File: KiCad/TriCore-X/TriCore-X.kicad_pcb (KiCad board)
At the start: 6 copper layers, 100 x 100 mm, 119 parts, among them J1 PJ-035DH, J2 877159106, J3 HDMI_A, Q1 AOD407, U1 RK3568B2, U10 USB3300-EZK-TR, U2 XC7A100T-FGG484, U3 TPS56637RPAR, U4 TPS56637RPAR, U5 RK809-5, U6 JFM38U1B-B313-4F, U7 STM32H723VGHx, U8 IS43LQ32256AL-062BLI, U9 TPD12S016RKTR, Y1 32.768KHZ, Y2 Crystal_GND24

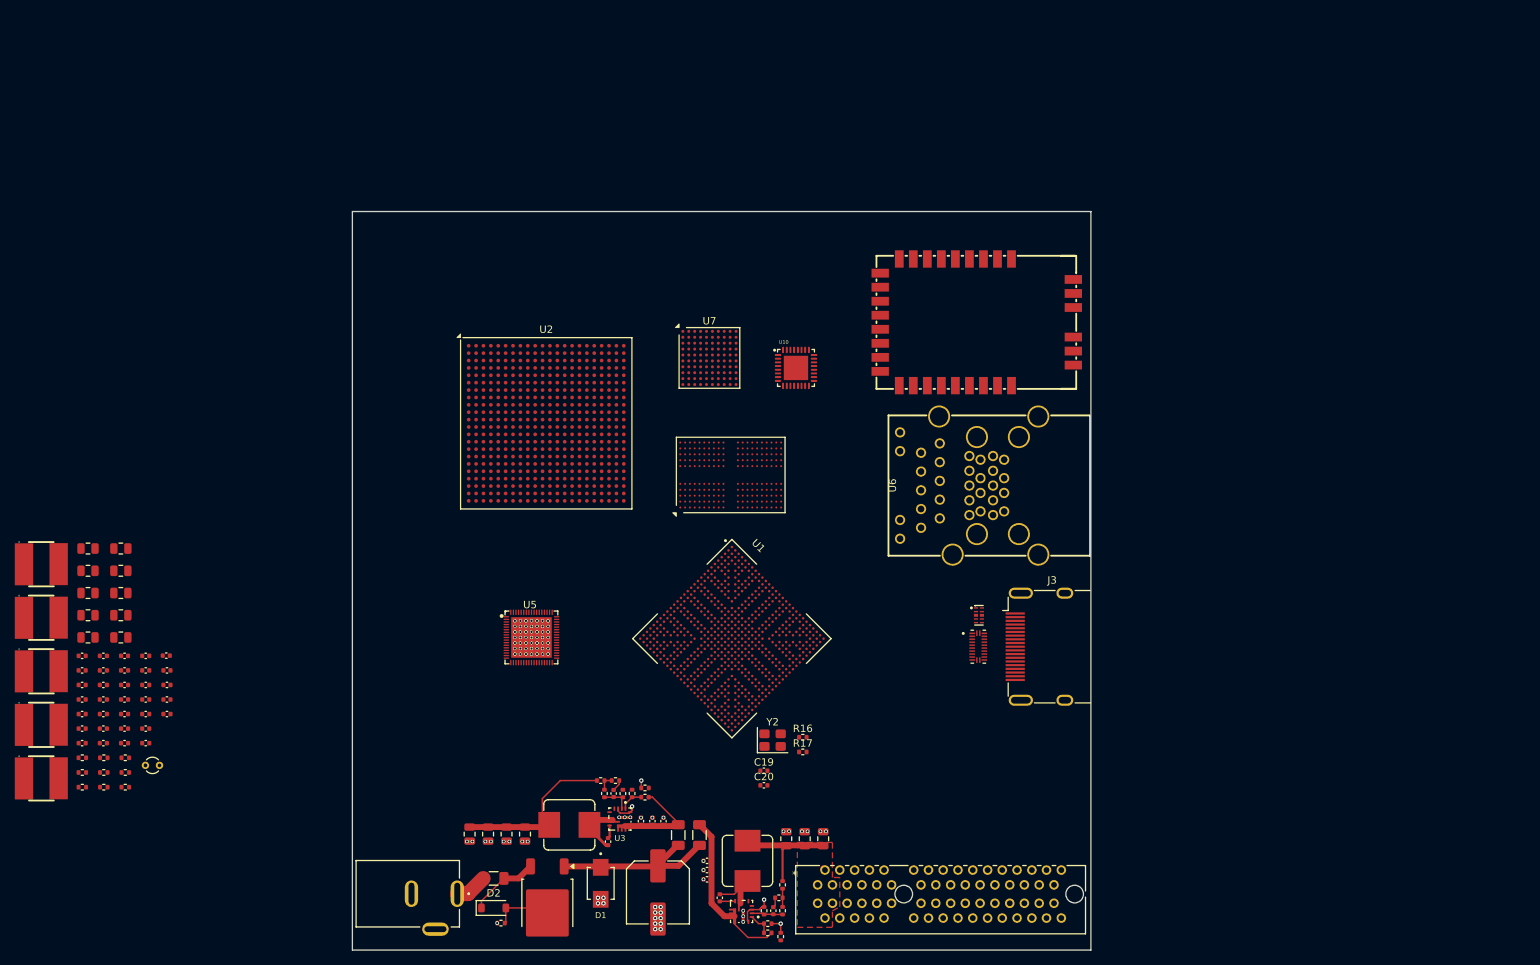
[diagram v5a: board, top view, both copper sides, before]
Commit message: refactor: update schematic components and library references, including STM32H743 and new power symbols
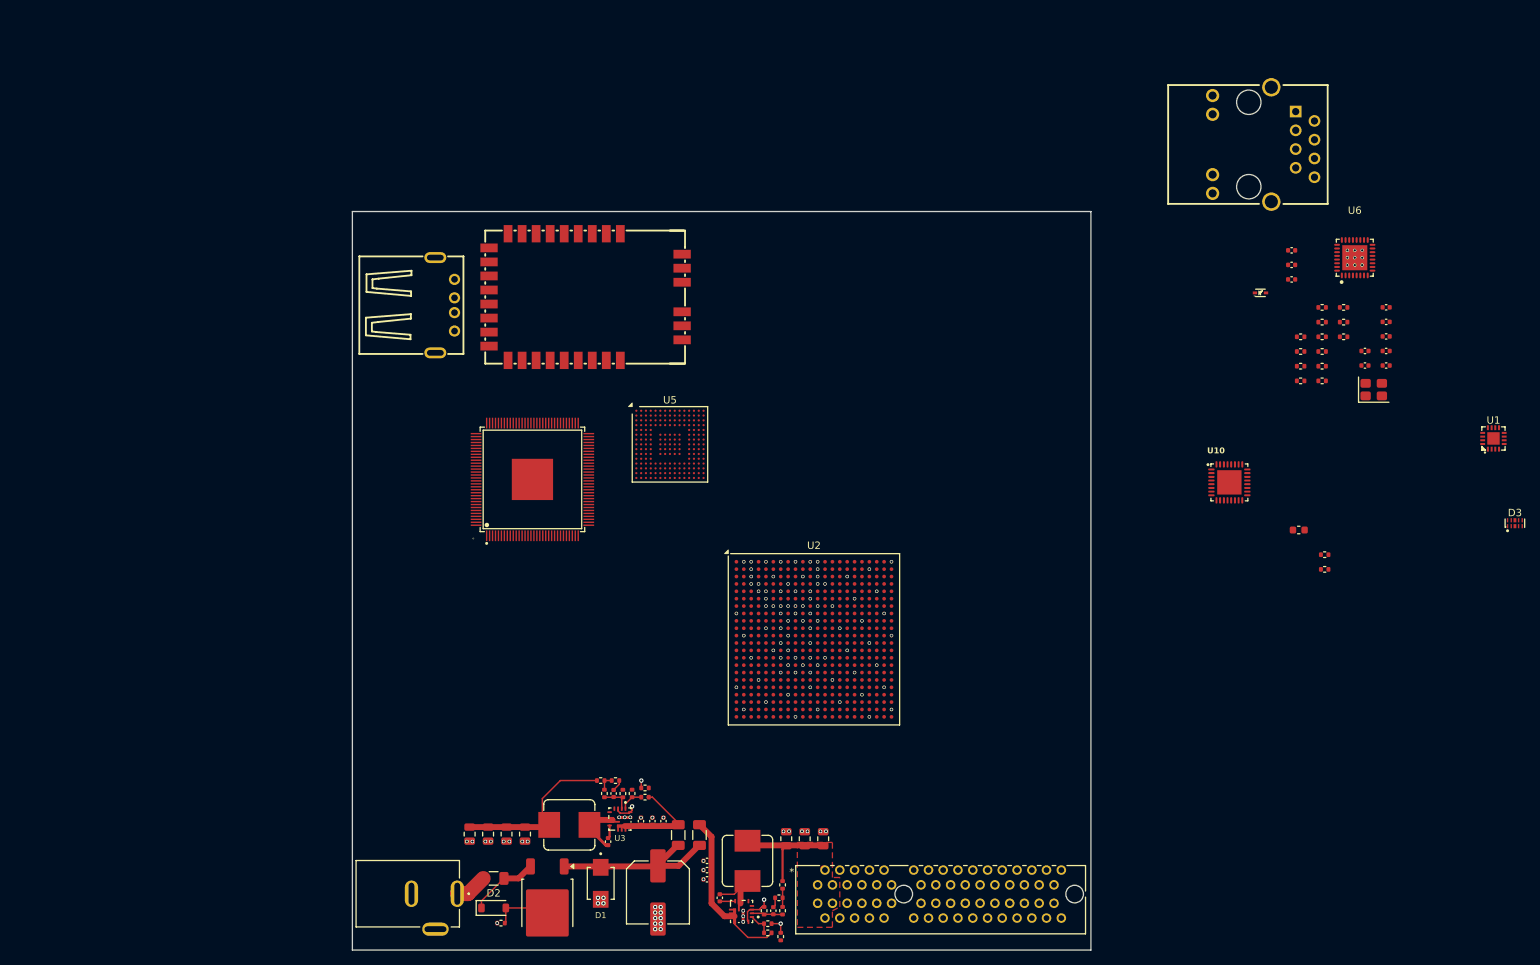
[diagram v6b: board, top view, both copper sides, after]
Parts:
- removed C29, C30, C31, C32, C33, C34, C35, C36, C37, C40, C41, C42, C43, C45: 1uF, Capacitor_SMD:C_0402_1005Metric
- removed C38, C39: 2.2uF, Capacitor_SMD:C_0402_1005Metric
- removed C44, C46, C47, C48, C49, C50: 10uF, Capacitor_SMD:C_0402_1005Metric
- removed C51, C52, C53, C54, C55, C56, C57, C58, C59, C60: 22uF, Capacitor_SMD:C_0805_2012Metric
- removed C61, C62, C63: 100nF, Capacitor_SMD:C_0402_1005Metric
- removed L3, L4, L5, L6, L7: FNR6045SR47NT, L_6045:IND-SMD_L6.0-W6.0_FNR60XXS
- removed U8: IS43LQ32256AL-062BLI, Package_BGA:BGA-200_10x14.5mm_Layout12x22_P0.8x0.65mm
- removed U9: TPD12S016RKTR, TPD12S016RKTR:IC_TPD12S016RKTR
- removed Y2: Crystal_GND24, Crystal:Crystal_SMD_3225-4Pin_3.2x2.5mm
- added D5: LESD5D5.0CT1G, LESD5D5.0CT1G:SOD-523_L1.2-W0.8-LS1.6-BI, F.Cu at (216.7, 56.8)
- added FB1: 220R@100M, Inductor_SMD:L_0603_1608Metric, F.Cu at (221.9, 89.0)
- added R27: 22R, Resistor_SMD:R_0402_1005Metric, F.Cu at (225.1, 68.8)
- added R28: 22R, Resistor_SMD:R_0402_1005Metric, F.Cu at (228.0, 58.8)
- added R29: 4.7k, Resistor_SMD:R_0402_1005Metric, F.Cu at (228.0, 60.8)
- added R30: 4.7k, Resistor_SMD:R_0402_1005Metric, F.Cu at (228.0, 62.8)
- added USB1: AF 90° ZJDG ZB, USB-A:USB-A-TH_AF-90-ZJDG-ZB, F.Cu at (101.8, 58.5)
- C14, C4: value 0.1uF -> 100nF
- C19: value 18pF -> 1nF/50V
- C20: value 18pF -> 10nF
- C21: value 1uF -> 10nF
- C22, C25, C27: value 1uF -> 100nF
- C23, C24: value 1uF -> 15pF
- C26, C28: value 1uF -> 10uF
- J3: value HDMI_A -> HR911105A_C12074; footprint Connector_Video:HDMI_A_Molex_208658-1001_Horizontal -> RJ45:RJ45-TH_HR911105A
- R16: value 1M -> 510R
- R17: value 22R -> 510R
- R18: value 82K -> 4.7k
- R19: value 120K -> 1.5k
- R20: value 4.7K -> 1.5k
- R21: value 4.7K -> 4.7k
- R22: value 100K -> 4.7k
- R23: value 22K -> 4.7k
- R24: value 10K -> 2.49k
- R25, R26: value 10K -> 22R
- U1: value RK3568B2 -> CH334P; footprint RK3568B2:BGA636C65P28X28_1900X1900X111 -> CH334P:QFN-16_L3.0-W3.0-P0.50-BL-EP1.7
- U5: value RK809-5 -> STM32H743IIKx; footprint RK809-5:QFN-68_L7.0-W7.0-P0.35-BL-EP5.5 -> Package_BGA:UFBGA-201_10x10mm_Layout15x15_P0.65mm
- U6: value JFM38U1B-B313-4F -> RTL8201F-VB-CG; footprint JFM38U1B-B313-4F:RJ45-TH_JFM38U11-B31X-4F -> RTL8201F-VB-CG:QFN-32_L5.0-W5.0-P0.50-BL-EP3.4
- U7: value STM32H723VGHx -> T113-S3_C5197687; footprint Package_BGA:TFBGA-100_8x8mm_Layout10x10_P0.8mm -> T113-S3:LQFP-128_L14.0-W14.0-P0.40-LS16.0-BL-EP5.6
- Y1: value 32.768KHZ -> 25Mhz; footprint Crystal:Crystal_DS26_D2.0mm_L6.0mm_Vertical -> Crystal:Crystal_SMD_3225-4Pin_3.2x2.5mm
- moved C24 184.4 mm to (233.7, 58.8)
- moved C25 184.4 mm to (233.7, 60.8)
- moved C26 184.4 mm to (233.7, 62.7)
- moved C27 184.4 mm to (233.7, 64.7)
- moved C22 179.0 mm to (230.9, 64.7)
- moved C23 179.0 mm to (230.9, 66.7)
- moved C28 178.1 mm to (233.7, 66.7)
- moved R22 176.6 mm to (225.1, 58.8)
- moved R23 176.6 mm to (225.1, 60.8)
- moved R18 174.5 mm to (222.2, 62.8)
- moved R19 174.5 mm to (222.2, 64.8)
- moved R20 174.5 mm to (222.2, 66.8)
- moved Y1 173.9 mm to (232.1, 69.9)
- moved R24 171.8 mm to (225.1, 62.8)
- moved R25 171.8 mm to (225.1, 64.8)
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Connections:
- C19 pad 1: Net-(C19-Pad1) -> GND
- C19 pad 2: GND -> Net-(J3-CHSGND)
- C20 pad 2: Net-(U1F-XIN24M) -> Net-(C20-Pad2)
- C21 pad 1: /power/VSWOUT2 -> GND
- C21 pad 2: GND -> Net-(C21-Pad2)
- C22 pad 1: /power/BUCK5 -> Net-(U6-DVDD10OUT)
- C23 pad 1: /power/VCC SYS -> GND
- C23 pad 2: GND -> Net-(U6-CKXTAL2)
- C24 pad 1: /power/VLDOI -> GND
- C24 pad 2: GND -> Net-(U6-CKXTAL1)
- C25 pad 1: /power/VLDO2 -> GND
- C25 pad 2: GND -> Net-(U6-AVDD10OUT)
- C26 pad 1: /power/VLDO3 -> Ethernet_3V3
- C27 pad 1: /power/BUCK 5 -> Ethernet_3V3
- C28 pad 1: /power/VLDO4 -> Ethernet_3V3
- J3 pad 1: unconnected-(J3-D2+-Pad1) -> /Expansion_Port/ETH_TX_P
- J3 pad 10: unconnected-(J3-CK+-Pad10) -> Net-(J3-Pad10)
- J3 pad 11: unconnected-(J3-CKS-Pad11) -> GND
- J3 pad 12: unconnected-(J3-CK--Pad12) -> Net-(J3-Pad12)
- J3 pad 2: unconnected-(J3-D2S-Pad2) -> /Expansion_Port/ETH_TX_N
- J3 pad 3: unconnected-(J3-D2--Pad3) -> /Expansion_Port/ETH_RX_P
- J3 pad 4: unconnected-(J3-D1+-Pad4) -> Net-(C20-Pad2)
- J3 pad 5: unconnected-(J3-D1S-Pad5) -> Net-(C21-Pad2)
- J3 pad 6: unconnected-(J3-D1--Pad6) -> /Expansion_Port/ETH_RX_N
- J3 pad 8: unconnected-(J3-D0S-Pad8) -> Net-(J3-CHSGND)
- J3 pad 9: unconnected-(J3-D0--Pad9) -> Ethernet_3V3
- R16 pad 1: Net-(U1F-XIN24M) -> /Expansion_Port/LED_ACT
- R16 pad 2: Net-(U1F-XOUT24M) -> Net-(J3-Pad10)
- R17 pad 1: Net-(U1F-XOUT24M) -> /Expansion_Port/LED_LINK
- R17 pad 2: Net-(C19-Pad1) -> Net-(J3-Pad12)
- R18 pad 1: Net-(U5-FB3) -> /Expansion_Port/LED_ACT
- R18 pad 2: /power/BUCK3 -> Ethernet_3V3
- R19 pad 1: GND -> PHY_MDIO
- R19 pad 2: Net-(U5-FB3) -> Ethernet_3V3
- R20 pad 1: /power/BUCK4 -> PHY_MDC
- R20 pad 2: /power/RK809-5_SCL -> Ethernet_3V3
- R21 pad 1: /power/BUCK4 -> PHY_RSTN
- R21 pad 2: /power/RK809-5_SDA -> Ethernet_3V3
- R22 pad 1: +5V -> PHY_RXER
- R22 pad 2: Net-(U5-VDC) -> GND
- R23 pad 1: Net-(U5-VDC) -> /Expansion_Port/LED_LINK
- R24 pad 1: /power/BUCK4 -> GND
- R24 pad 2: Net-(U5-INT) -> Net-(U6-RSET)
- R25 pad 1: Net-(U5-CLK32K) -> /Expansion_Port/ETH_TX_P
- R25 pad 2: /power/BUCK4 -> Net-(U6-MDI+[0])
- R26 pad 1: Net-(U5-RESETB) -> /Expansion_Port/ETH_TX_N
- R26 pad 2: /power/BUCK4 -> Net-(U6-MDI-[0])
- U6 pad 1: unconnected-(U6-VBUS-Pad1) -> Net-(U6-RSET)
- U6 pad 10: unconnected-(U6-VBUS-Pad10) -> PHY_RXD1
- U6 pad 13: GND -> unconnected-(U6-RXC-Pad13)
- U6 pad 14: unconnected-(U6-STDA_SSRX--Pad14) -> Ethernet_3V3
- U6 pad 15: unconnected-(U6-STDA_SSRX+-Pad15) -> PHY_TXCLK
- U6 pad 16: GND -> PHY_TXD0
- U6 pad 17: unconnected-(U6-SRDA_SSTX--Pad17) -> PHY_TXD1
- U6 pad 2: unconnected-(U6-D--Pad2) -> Net-(U6-AVDD10OUT)
- U6 pad 20: unconnected-(U6-D1+-Pad20) -> PHY_TXEN
- U6 pad 21: unconnected-(U6-D1--Pad21) -> PHY_RSTN
- U6 pad 22: unconnected-(U6-D2+-Pad22) -> PHY_MDC
- U6 pad 23: unconnected-(U6-D2--Pad23) -> PHY_MDIO
- U6 pad 24: unconnected-(U6-D3+-Pad24) -> /Expansion_Port/LED_ACT
- U6 pad 25: unconnected-(U6-D3--Pad25) -> /Expansion_Port/LED_LINK
- U6 pad 26: unconnected-(U6-D4+-Pad26) -> PHY_CRS_DV
- U6 pad 28: GND -> PHY_RXER
- U6 pad 29: unconnected-(U6-LED-G+-Pad29) -> Net-(U6-DVDD10OUT)
- U6 pad 3: unconnected-(U6-D+-Pad3) -> Net-(U6-MDI+[0])
- U6 pad 30: unconnected-(U6-LED-D--Pad30) -> Ethernet_3V3
- U6 pad 31: unconnected-(U6-LED-Y+-Pad31) -> Net-(U6-CKXTAL1)
- U6 pad 32: unconnected-(U6-LED-Y--Pad32) -> Net-(U6-CKXTAL2)
- U6 pad 33: unconnected-(U6-SHELL-Pad33) -> GND
- U6 pad 4: GND -> Net-(U6-MDI-[0])
- U6 pad 5: unconnected-(U6-STDA_SSRX--Pad5) -> Net-(U6-MDI+[1])
- U6 pad 6: unconnected-(U6-STDA_SSRX+-Pad6) -> Net-(U6-MDI-[1])
- U6 pad 7: GND -> Ethernet_3V3
- U6 pad 8: unconnected-(U6-SRDA_SSTX--Pad8) -> Net-(U6-RXDV)
- U6 pad 9: unconnected-(U6-STDA_SSTX+-Pad9) -> PHY_RXD0
- Y1 pad 1: Net-(U5-XOUT) -> Net-(U6-CKXTAL1)
- Y1 pad 2: Net-(U5-XIN) -> GND
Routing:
- net GND: vias 90 -> 137

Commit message: refactor: update schematic components, remove unused files, and add new LED and CH334P symbols
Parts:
- removed WIFI1: BL-M8822CU3-A, BL-M8822CU3-A:WIRELM-SMD_BL-M8822CU3-A
- added B1: CR2032-BS-2-1, Battery Holder BS-2-1:BAT-TH_BS-2-1, F.Cu at (121.8, 30.0)
- added C29: 22uF, Capacitor_SMD:C_0805_2012Metric, F.Cu at (124.8, 108.7)
- added C30: 100nF, Capacitor_SMD:C_0402_1005Metric, F.Cu at (121.5, 112.2)
- added C31: 22uF, Capacitor_SMD:C_0805_2012Metric, F.Cu at (119.8, 112.2)
- added C32: 22uF, Capacitor_SMD:C_0805_2012Metric, F.Cu at (119.5, 103.9)
- added C33: 100nF, Capacitor_SMD:C_0402_1005Metric, F.Cu at (121.3, 104.2)
- added C34: 22uF, Capacitor_SMD:C_0805_2012Metric, F.Cu at (124.8, 100.4)
- added C35: 22uF, Capacitor_SMD:C_0805_2012Metric, F.Cu at (119.5, 94.9)
- added C36: 100nF, Capacitor_SMD:C_0402_1005Metric, F.Cu at (121.2, 95.0)
- added C37: 22uF, Capacitor_SMD:C_0805_2012Metric, F.Cu at (124.7, 91.5)
- added C38: 22uF, Capacitor_SMD:C_0805_2012Metric, F.Cu at (119.7, 86.9)
- added C39: 100nF, Capacitor_SMD:C_0402_1005Metric, F.Cu at (121.5, 87.1)
- added C40: 22uF, Capacitor_SMD:C_0805_2012Metric, F.Cu at (125.0, 83.5)
- added C41: 1uF, Capacitor_SMD:C_0402_1005Metric, F.Cu at (104.2, 91.8)
- added C42: 1uF, Capacitor_SMD:C_0402_1005Metric, F.Cu at (100.5, 91.9)
- added C43: 1uF, Capacitor_SMD:C_0402_1005Metric, F.Cu at (104.2, 86.2)
- added C44: 1uF, Capacitor_SMD:C_0402_1005Metric, F.Cu at (100.5, 86.2)
- added C45: 22uF, Capacitor_SMD:C_0805_2012Metric, F.Cu at (122.0, 108.0)
- added C46: 22uF, Capacitor_SMD:C_0805_2012Metric, F.Cu at (122.0, 99.7)
- added C47: 22uF, Capacitor_SMD:C_0805_2012Metric, F.Cu at (122.0, 90.8)
- added C48: 22uF, Capacitor_SMD:C_0805_2012Metric, F.Cu at (122.2, 82.8)
- added C49: 100nF, Capacitor_SMD:C_0402_1005Metric, F.Cu at (146.0, 27.6)
- added C50: 2.2uF, Capacitor_SMD:C_0402_1005Metric, F.Cu at (146.0, 29.5)
- added C51: 2.2uF, Capacitor_SMD:C_0402_1005Metric, F.Cu at (146.0, 31.5)
- added C52: 100nF, Capacitor_SMD:C_0402_1005Metric, B.Cu at (150.8, 53.3)
- added C53: 100nF, Capacitor_SMD:C_0402_1005Metric, F.Cu at (146.0, 33.5)
- added C54: 1uF, Capacitor_SMD:C_0402_1005Metric, F.Cu at (146.0, 35.4)
- added C55: 100nF, Capacitor_SMD:C_0402_1005Metric, B.Cu at (150.8, 55.2)
- added C56: 100nF, Capacitor_SMD:C_0402_1005Metric, B.Cu at (150.8, 57.2)
- added C57: 100nF, Capacitor_SMD:C_0402_1005Metric, B.Cu at (150.8, 59.2)
- added C58: 100nF, Capacitor_SMD:C_0402_1005Metric, B.Cu at (150.8, 61.2)
- added C59: 100nF, Capacitor_SMD:C_0402_1005Metric, B.Cu at (147.9, 53.3)
- added C60: 100nF, Capacitor_SMD:C_0402_1005Metric, B.Cu at (147.9, 55.2)
- added C61: 100nF, Capacitor_SMD:C_0402_1005Metric, B.Cu at (147.9, 57.2)
- added C62: 100nF, Capacitor_SMD:C_0402_1005Metric, B.Cu at (147.9, 59.2)
- added C63: 100nF, Capacitor_SMD:C_0402_1005Metric, B.Cu at (147.9, 61.2)
- added C64: 100nF, Capacitor_SMD:C_0402_1005Metric, B.Cu at (145.0, 53.3)
- added C65: 100nF, Capacitor_SMD:C_0402_1005Metric, B.Cu at (145.0, 55.2)
- added C66: 100nF, Capacitor_SMD:C_0402_1005Metric, B.Cu at (145.0, 57.2)
- added C67: 100nF, Capacitor_SMD:C_0402_1005Metric, B.Cu at (145.0, 59.2)
- added C68: 100nF, Capacitor_SMD:C_0402_1005Metric, B.Cu at (145.0, 61.2)
- added C69: 100nF, Capacitor_SMD:C_0402_1005Metric, B.Cu at (142.2, 53.3)
- added C70: 100nF, Capacitor_SMD:C_0402_1005Metric, B.Cu at (142.2, 55.2)
- added C71: 100nF, Capacitor_SMD:C_0402_1005Metric, B.Cu at (142.2, 57.2)
- added C72: 100nF, Capacitor_SMD:C_0402_1005Metric, B.Cu at (141.8, 59.8)
- added C73: 100nF, Capacitor_SMD:C_0402_1005Metric, B.Cu at (141.0, 61.2)
- added C74: 100nF, Capacitor_SMD:C_0402_1005Metric, B.Cu at (138.0, 61.5)
- added D10: LED, LED_SMD:LED_0603_1608Metric, F.Cu at (68.5, 85.2)
- added D11: SS14, Diode_SMD:D_SMA, F.Cu at (106.2, 38.0)
- added D4: ESD224DQAR, ESD224DQAR:USON-10_L2.5-W1.0-P0.50-BL, F.Cu at (104.8, 75.8)
- added D6: LED, LED_SMD:LED_0603_1608Metric, F.Cu at (68.5, 74.8)
- added D7: LED, LED_SMD:LED_0603_1608Metric, F.Cu at (68.5, 77.4)
- added D8: LED, LED_SMD:LED_0603_1608Metric, F.Cu at (68.5, 80.0)
- added D9: LED, LED_SMD:LED_0603_1608Metric, F.Cu at (68.5, 82.6)
- added L3: FWP252012P-1R0ML, FWP252012P-1R0ML:IND-SMD_L2.5-W2.0_YXMBL252010P, F.Cu at (124.0, 113.0)
- added L4: FWP252012P-1R0ML, FWP252012P-1R0ML:IND-SMD_L2.5-W2.0_YXMBL252010P, F.Cu at (124.0, 104.7)
- added L5: FWP252012P-1R0ML, FWP252012P-1R0ML:IND-SMD_L2.5-W2.0_YXMBL252010P, F.Cu at (124.0, 95.8)
- added L6: FWP252012P-1R0ML, FWP252012P-1R0ML:IND-SMD_L2.5-W2.0_YXMBL252010P, F.Cu at (124.2, 87.6)
- added R31: 68K, Resistor_SMD:R_0402_1005Metric, F.Cu at (126.5, 110.3)
- added R32: 20K, Resistor_SMD:R_0402_1005Metric, F.Cu at (126.5, 102.0)
- added R33: 15K, Resistor_SMD:R_0402_1005Metric, F.Cu at (126.5, 108.3)
- added R34: 30K, Resistor_SMD:R_0402_1005Metric, F.Cu at (126.5, 100.0)
- added R35: 30K, Resistor_SMD:R_0402_1005Metric, F.Cu at (126.7, 85.0)
- added R36: 30K, Resistor_SMD:R_0402_1005Metric, F.Cu at (84.7, 83.6)
- added R37: 15K, Resistor_SMD:R_0402_1005Metric, F.Cu at (126.5, 93.0)
- added R38: 20K, Resistor_SMD:R_0402_1005Metric, F.Cu at (126.7, 83.0)
- added R39: 30K, Resistor_SMD:R_0402_1005Metric, F.Cu at (125.2, 124.2)
- added R40: 49.9R, Resistor_SMD:R_0402_1005Metric, F.Cu at (55.0, 76.5)
- added R41: 49.9R, Resistor_SMD:R_0402_1005Metric, F.Cu at (55.0, 78.5)
- added R42: 49.9R, Resistor_SMD:R_0402_1005Metric, F.Cu at (55.0, 80.5)
- added R43: 49.9R, Resistor_SMD:R_0402_1005Metric, F.Cu at (55.0, 82.5)
- added R44: 49.9R, Resistor_SMD:R_0402_1005Metric, F.Cu at (55.0, 84.5)
- added R45: 30K, Resistor_SMD:R_0402_1005Metric, F.Cu at (87.6, 85.5)
- added R46: 30K, Resistor_SMD:R_0402_1005Metric, F.Cu at (86.7, 76.3)
- added R47: 30K, Resistor_SMD:R_0402_1005Metric, F.Cu at (126.5, 91.0)
- added R48: 30K, Resistor_SMD:R_0402_1005Metric, F.Cu at (86.7, 80.2)
- added R49: 30K, Resistor_SMD:R_0402_1005Metric, F.Cu at (57.9, 80.5)
- added R50: 30K, Resistor_SMD:R_0402_1005Metric, F.Cu at (57.9, 82.5)
- added R51: 30K, Resistor_SMD:R_0402_1005Metric, F.Cu at (57.9, 84.5)
- added R52: 30K, Resistor_SMD:R_0402_1005Metric, F.Cu at (57.9, 86.5)
- added R53: 30K, Resistor_SMD:R_0402_1005Metric, F.Cu at (120.0, 101.4)
- added R54: 30K, Resistor_SMD:R_0402_1005Metric, F.Cu at (119.7, 92.5)
- added R55: 30K, Resistor_SMD:R_0402_1005Metric, F.Cu at (120.0, 84.4)
- added R56: 30K, Resistor_SMD:R_0402_1005Metric, F.Cu at (105.8, 92.2)
- added R57: 30K, Resistor_SMD:R_0402_1005Metric, F.Cu at (102.0, 92.4)
- added REF**: MountingHole_4.3mm_M4, MountingHole:MountingHole_4.3mm_M4, F.Cu at (102.0, 124.0)
- added U11: RT9013-18GB, RT9013-18GB:SOT-23-5_L3.0-W1.7-P0.95-LS2.8-BR, F.Cu at (104.8, 89.0)
- added U12: RT9013-12GB, RT9013-12GB:SOT-23-5_L3.0-W1.7-P0.95-LS2.8-BR, F.Cu at (101.0, 89.0)
- added U13: TPS22966DPUR, TPS22966DPUR:WSON-14_L3.0-W2.0-P0.40-BL-EP, F.Cu at (56.8, 68.9)
- added U14: TPS22966DPUR, TPS22966DPUR:WSON-14_L3.0-W2.0-P0.40-BL-EP, F.Cu at (61.1, 68.9)
- added U15: TPS22966DPUR, TPS22966DPUR:WSON-14_L3.0-W2.0-P0.40-BL-EP, F.Cu at (65.4, 68.9)
- added U16: TPS22966DPUR, TPS22966DPUR:WSON-14_L3.0-W2.0-P0.40-BL-EP, F.Cu at (69.7, 69.0)
- added U17: CH334P, CH334P:QFN-16_L3.0-W3.0-P0.50-BL-EP1.7, F.Cu at (206.6, 103.4)
- added U8: SY8843QWC, SY8843QWC:QFN-7_L1.5-W1.5-P0.45-BL_SILERGY_SY8842QWC, F.Cu at (122.5, 102.0)
- added U9: SY8843QWC, SY8843QWC:QFN-7_L1.5-W1.5-P0.45-BL_SILERGY_SY8842QWC, F.Cu at (122.5, 93.0)
- U1: value CH334P -> XC7A35T-CSG325; footprint CH334P:QFN-16_L3.0-W3.0-P0.50-BL-EP1.7 -> Package_BGA:Xilinx_CSG325
- U10: value USB3300-EZK-TR -> SY8843QWC; footprint USB3300-EZK-TR:QFN50P500X500X100-33N -> SY8843QWC:QFN-7_L1.5-W1.5-P0.45-BL_SILERGY_SY8842QWC
- U2: value XC7A100T-FGG484 -> V851S; footprint Package_BGA:BGA-484_23.0x23.0mm_Layout22x22_P1.0mm -> V851s:QFN-88_L9.0-W9.0-P0.35-TL-EP6.5
- U5: value STM32H743IIKx -> STM32H745XIHx; footprint Package_BGA:UFBGA-201_10x10mm_Layout15x15_P0.65mm -> Package_BGA:TFBGA-265_14x14mm_Layout17x17_P0.8mm
- U7: value T113-S3_C5197687 -> SY8843QWC; footprint T113-S3:LQFP-128_L14.0-W14.0-P0.40-LS16.0-BL-EP5.6 -> SY8843QWC:QFN-7_L1.5-W1.5-P0.45-BL_SILERGY_SY8842QWC
- moved U10 89.8 mm to (122.7, 85.1), turned to -90 degrees
- moved U1 74.4 mm to (175.2, 90.8)
- moved U7 28.3 mm to (122.5, 110.2), turned to -90 degrees
- moved U2 16.4 mm to (147.5, 89.9)
- moved C9 12.1 mm to (116.2, 120.0), turned to 180 degrees
- moved C8 8.67 mm to (116.2, 122.5), turned to 180 degrees
- moved U5 8.32 mm to (142.9, 71.8)
- moved C7 5.38 mm to (116.2, 125.0), turned to 180 degrees
- moved C6 2.77 mm to (116.2, 127.5), turned to 180 degrees
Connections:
- U10 pad 1: unconnected-(U10-GND-1-Pad1) -> Net-(U10-FB)
- U10 pad 2: GND -> +1.5V
- U10 pad 3: unconnected-(U10-CPEN-Pad3) -> 1.5V_OK
- U10 pad 4: unconnected-(U10-VBUS-Pad4) -> Net-(U10-EN)
- U10 pad 5: unconnected-(U10-ID-Pad5) -> +5V
- U10 pad 6: unconnected-(U10-VDD3.3-3-Pad6) -> Net-(U10-LX)
- U10 pad 7: unconnected-(U10-DP-Pad7) -> GND
- U5 pad A1: unconnected-(U5-PE3-PadA1) -> GND
- U5 pad A6: unconnected-(U5-PB5-PadA6) -> Net-(U5-VDDLDO-PadA6)
- U5 pad A7: unconnected-(U5-PG14-PadA7) -> Net-(C50-Pad2)
- U5 pad B1: unconnected-(U5-PE4-PadB1) -> Net-(D11-K)
- U5 pad B2: unconnected-(U5-PE5-PadB2) -> GND
- U5 pad B6: unconnected-(U5-PB6-PadB6) -> GND
- U5 pad C10: unconnected-(U5-PG9-PadC10) -> GND
- U5 pad C13: unconnected-(U5-PI3-PadC13) -> GND
- U5 pad D5: GND -> unconnected-(U5-PB8-PadD5)
- U5 pad D7: GND -> unconnected-(U5-PK7-PadD7)
- U5 pad D8: GND -> unconnected-(U5-PG14-PadD8)
- U5 pad D9: GND -> unconnected-(U5-PG13-PadD9)
- U5 pad F1: unconnected-(U5-PC15-PadF1) -> GND
- U5 pad F2: GND -> unconnected-(U5-VSSSMPS-PadF2)
- U5 pad G13: unconnected-(U5-VDD-PadG13) -> +3.3V
- U5 pad G2: GND -> unconnected-(U5-VFBSMPS-PadG2)
- U5 pad H13: unconnected-(U5-VDD33_USB-PadH13) -> +3.3V
- U5 pad J13: unconnected-(U5-VDD-PadJ13) -> +3.3V
- U5 pad J3: unconnected-(U5-PF4-PadJ3) -> GND
- U5 pad K13: unconnected-(U5-PG5-PadK13) -> +3.3V
- U5 pad K15: unconnected-(U5-PG3-PadK15) -> GND
- U5 pad L13: unconnected-(U5-PH10-PadL13) -> +3.3V
- U5 pad L15: unconnected-(U5-PG2-PadL15) -> GND
- U5 pad L4: GND -> unconnected-(U5-PF9-PadL4)
- U5 pad M1: GND -> VDDA
- U5 pad M13: unconnected-(U5-PH9-PadM13) -> +3.3V
- U5 pad M15: unconnected-(U5-PD13-PadM15) -> GND
- U5 pad M5: unconnected-(U5-PC3_C-PadM5) -> +3.3V
- U5 pad N10: unconnected-(U5-VDD-PadN10) -> +3.3V
- U5 pad N11: unconnected-(U5-PE13-PadN11) -> +3.3V
- U5 pad N12: unconnected-(U5-PH7-PadN12) -> +3.3V
- U5 pad N7: unconnected-(U5-PG0-PadN7) -> +3.3V
- U5 pad N8: unconnected-(U5-VDD-PadN8) -> +3.3V
- U5 pad R4: unconnected-(U5-PB1-PadR4) -> GND
- U5 pad R8: unconnected-(U5-PE7-PadR8) -> GND
- U7 pad 1: unconnected-(U7-PG6-Pad1) -> Net-(U7-FB)
- U7 pad 2: unconnected-(U7-PG7-Pad2) -> /power/SY8843_3.3V_OUT
- U7 pad 3: unconnected-(U7-PG8-Pad3) -> 3.3V_OK
- U7 pad 4: unconnected-(U7-PG9-Pad4) -> 5V_OK
- U7 pad 5: unconnected-(U7-PG10-Pad5) -> +5V
- U7 pad 6: unconnected-(U7-PG11-Pad6) -> Net-(U7-LX)
- U7 pad 7: unconnected-(U7-PF0-Pad7) -> GND
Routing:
- net GND: track 0.00 -> 6.19 mm, vias 137 -> 197
- net Net-(U9-FB): track 0.00 -> 4.93 mm, vias 0 -> 2
- net Net-(U8-FB): track 0.00 -> 4.93 mm, vias 0 -> 2
- net Net-(U7-FB): track 0.00 -> 4.93 mm, vias 0 -> 2
- net Net-(U10-FB): track 0.00 -> 4.93 mm, vias 0 -> 2
- net /power/SY8843_3.3V_OUT: track 0.00 -> 2.96 mm
- net Net-(U9-LX): track 0.00 -> 2.37 mm
- net Net-(U8-LX): track 0.00 -> 2.37 mm
- net Net-(U7-LX): track 0.00 -> 2.37 mm
- net Net-(U10-LX): track 0.00 -> 2.37 mm
- net Net-(U11-EN): track 0.00 -> 1.48 mm
- net Net-(U12-EN): track 0.00 -> 1.48 mm
- net +1V8: track 0.00 -> 1.44 mm
- net +1V2: track 0.00 -> 1.44 mm
- net +5V: track 23.2 -> 24.2 mm, vias 0 -> 9
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- added copper zone on F.Cu, net +0.9V
- added copper zone on F.Cu, net +1.5V
- added copper zone on F.Cu, net +1V
- added copper zone on F.Cu, net +5V
- added copper zone on F.Cu, net /power/SY8843_3.3V_OUT
- added copper zone on F.Cu, net GND
- added copper zone on F.Cu, net Net-(U10-LX)
- added copper zone on F.Cu, net Net-(U7-LX)
- added copper zone on F.Cu, net Net-(U8-LX)
- added copper zone on F.Cu, net Net-(U9-LX)
